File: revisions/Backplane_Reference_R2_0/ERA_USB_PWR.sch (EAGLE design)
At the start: 1 part

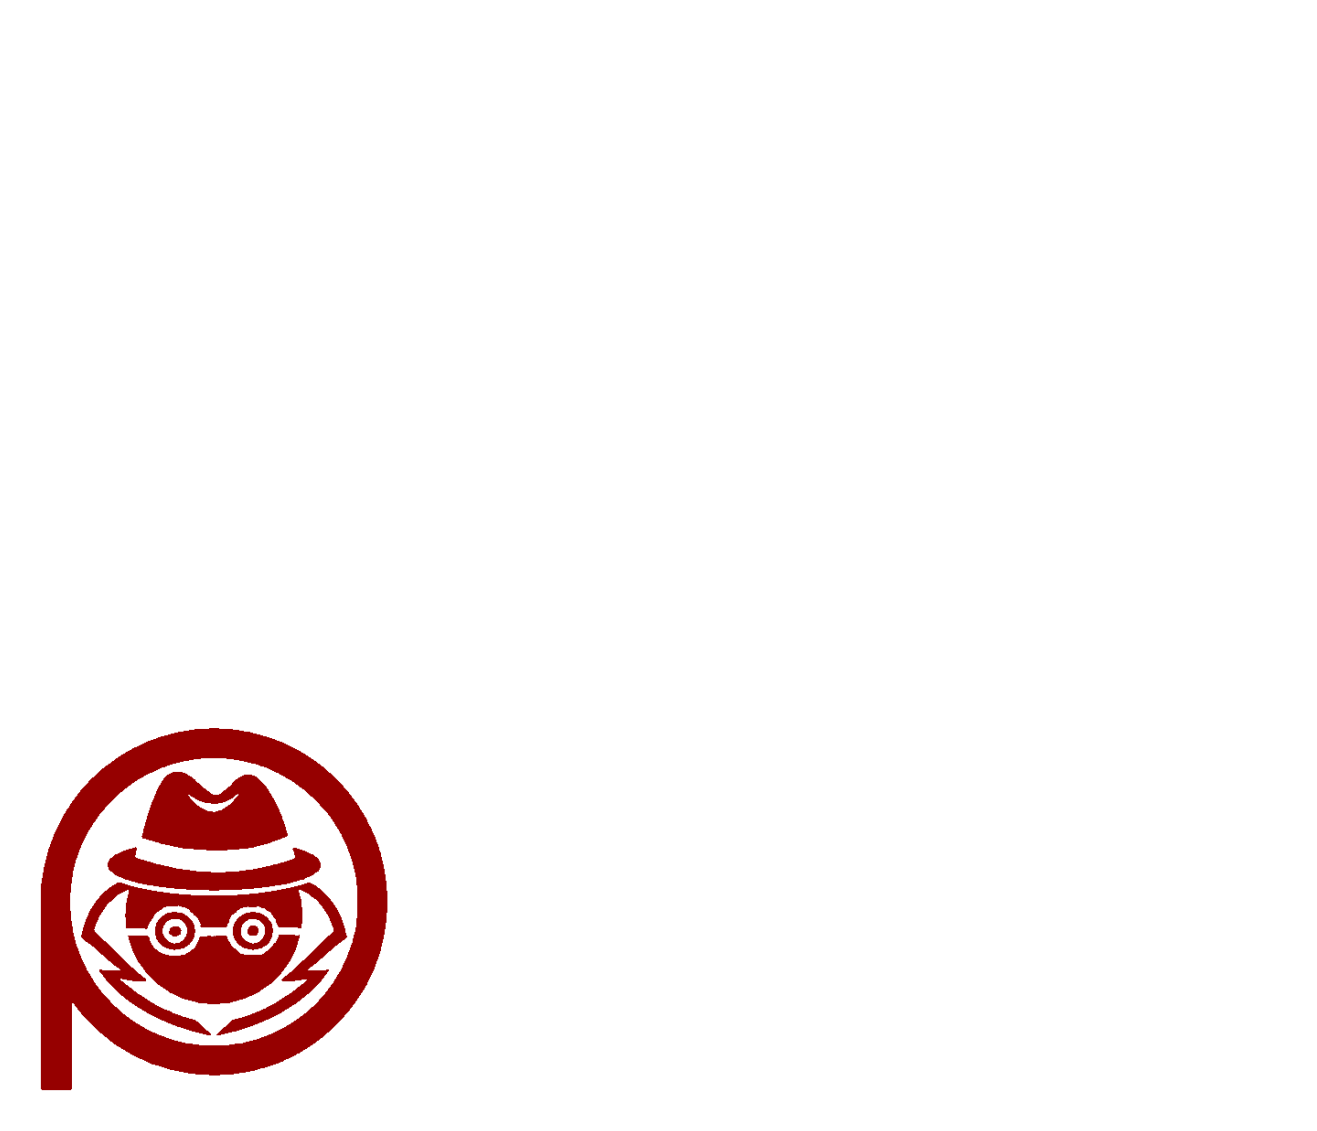
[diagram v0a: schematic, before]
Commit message: Enlarge SwitchMult Front panel holes for easier assembly/operation
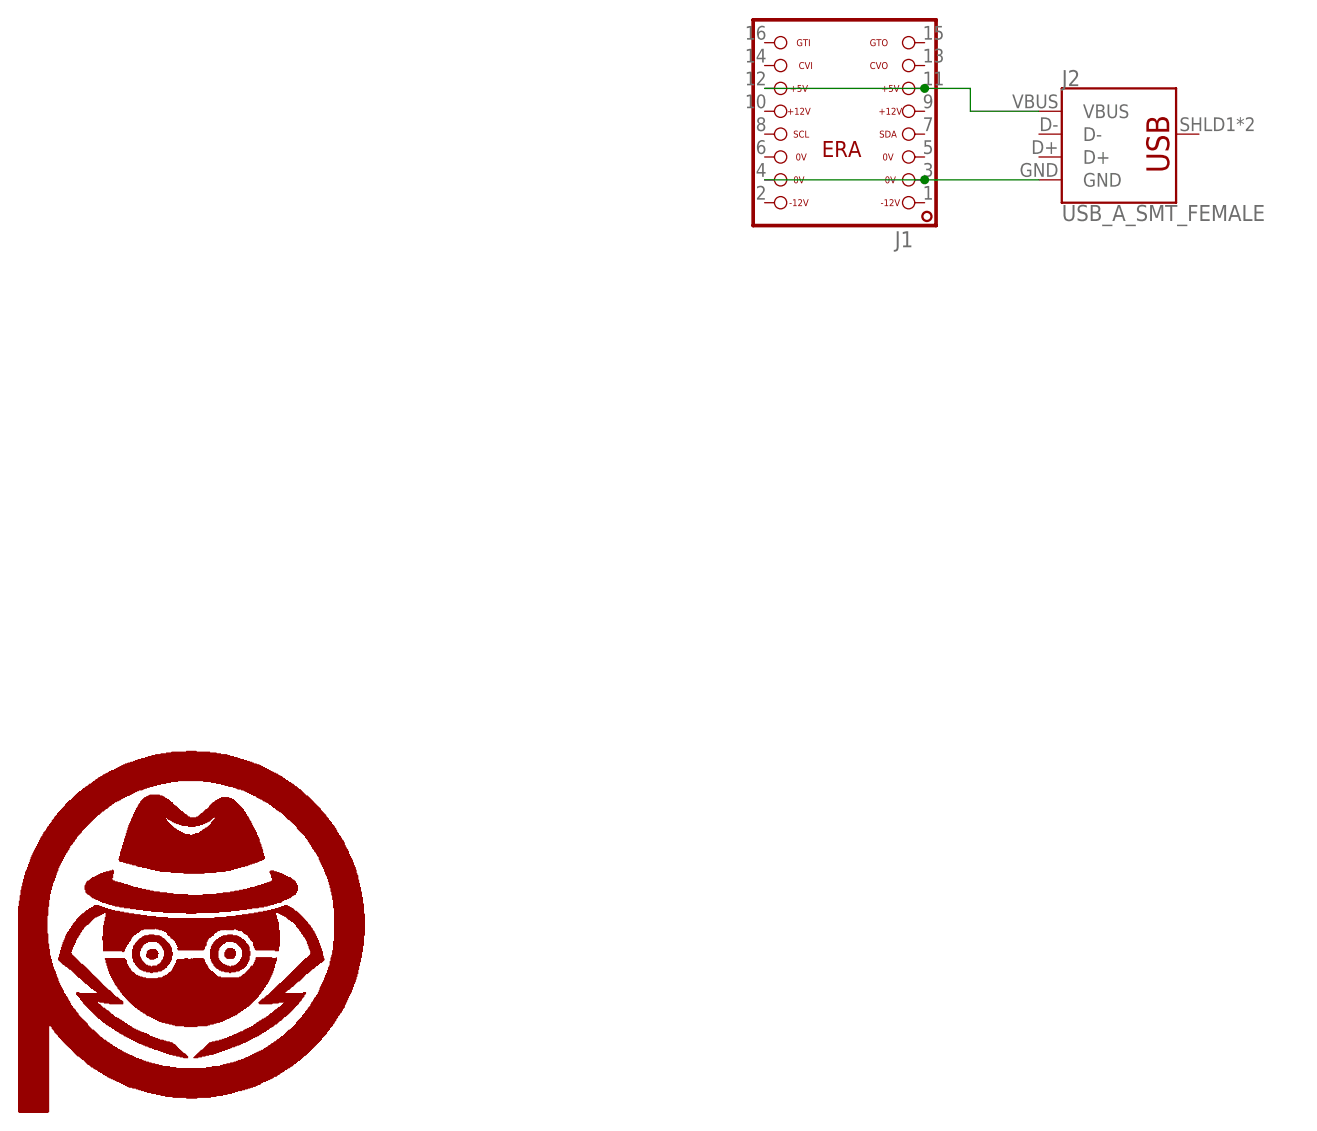
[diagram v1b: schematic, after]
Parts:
- added J1: ERA_16PIN-NOSILK, ERA:ERA_16PIN-NOSILK
- added J2: USB_A_SMT_FEMALE, SparkFun-Connectors:USB_A_SMT_FEMALE
- added U$2: PA_LOGO_SYMSMALL, PatternAgents-Logos:PA_LOGO_SYMSMALL
- U$1: value PA_LOGO_SYMLARGE -> PA_LOGO_SYMSMALL; device PatternAgents-Logos:PA_LOGO_SYMLARGE -> PatternAgents-Logos:PA_LOGO_SYMSMALL
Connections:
- new net GND: J1.3, J1.4, J2.GND
- new net N$2: J1.11, J1.12, J2.VBUS
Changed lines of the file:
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@@
 <layer number="2" name="Route2" color="1" fill="3" visible="no" active="no"/>
 <layer number="3" name="Route3" color="4" fill="3" visible="no" active="no"/>
+<layer number="4" name="Route4" color="1" fill="4" visible="no" active="no"/>
+<layer number="5" name="Route5" color="4" fill="4" visible="no" active="no"/>
+<layer number="6" name="Route6" color="1" fill="8" visible="no" active="no"/>
+<layer number="7" name="Route7" color="4" fill="8" visible="no" active="no"/>
+<layer number="8" name="Route8" color="1" fill="2" visible="no" active="no"/>
+<layer number="9" name="Route9" color="4" fill="2" visible="no" active="no"/>
+<layer number="10" name="Route10" color="1" fill="7" visible="no" active="no"/>
+<layer number="11" name="Route11" color="4" fill="7" visible="no" active="no"/>
+<layer number="12" name="Route12" color="1" fill="5" visible="no" active="no"/>
+<layer number="13" name="Route13" color="4" fill="5" visible="no" active="no"/>
 <layer number="14" name="Route14" color="1" fill="6" visible="no" active="no"/>
 <layer number="15" name="Route15" color="4" fill="6" visible="no" active="no"/>
@@
 <layer number="56" name="wert" color="7" fill="1" visible="no" active="no"/>
 <layer number="57" name="tCAD" color="7" fill="1" visible="no" active="no"/>
-<layer number="58" name="bCAD" color="11" fill="1" visible="no" active="no"/>
 <layer number="59" name="tCarbon" color="7" fill="1" visible="no" active="no"/>
 <layer number="60" name="bCarbon" color="7" fill="1" visible="no" active="no"/>
@@
 <layer number="97" name="Info" color="7" fill="1" visible="yes" active="yes"/>
 <layer number="98" name="Guide" color="6" fill="1" visible="yes" active="yes"/>
-<layer number="99" name="SpiceOrder" color="5" fill="1" visible="no" active="yes"/>
+<layer number="99" name="SpiceOrder" color="7" fill="1" visible="yes" active="yes"/>
 <layer number="100" name="Muster" color="7" fill="1" visible="no" active="yes"/>
 <layer number="101" name="Patch_Top" color="7" fill="1" visible="no" active="yes"/>
@@
 <layer number="115" name="ReferenceISLANDS" color="7" fill="1" visible="yes" active="yes"/>
 <layer number="116" name="Patch_BOT" color="7" fill="1" visible="no" active="yes"/>
-<layer number="117" name="BACKMAAT1" color="7" fill="1" visible="no" active="no"/>
 <layer number="118" name="Rect_Pads" color="7" fill="1" visible="yes" active="yes"/>
-<layer number="119" name="KAP_TEKEN" color="7" fill="1" visible="no" active="no"/>
-<layer number="120" name="KAP_MAAT1" color="7" fill="1" visible="no" active="no"/>
 <layer number="121" name="_tsilk" color="7" fill="1" visible="no" active="yes"/>
 <layer number="122" name="_bsilk" color="7" fill="1" visible="no" active="yes"/>
@@
 <layer number="128" name="_bValues" color="7" fill="1" visible="no" active="yes"/>
 <layer number="129" name="Mask" color="7" fill="1" visible="yes" active="yes"/>
-<layer number="130" name="SMDSTROOK" color="7" fill="1" visible="no" active="no"/>
 <layer number="131" name="tAdjust" color="7" fill="1" visible="no" active="yes"/>
 <layer number="132" name="bAdjust" color="7" fill="1" visible="no" active="yes"/>
-<layer number="133" name="bottom_silk" color="7" fill="1" visible="no" active="no"/>
-<layer number="134" name="silk_top" color="7" fill="1" visible="no" active="no"/>
-<layer number="135" name="silk_bottom" color="7" fill="1" visible="no" active="no"/>
-<layer number="136" name="silktop" color="7" fill="1" visible="yes" active="yes"/>
-<layer number="137" name="silkbottom" color="7" fill="1" visible="yes" active="yes"/>
 <layer number="144" name="Drill_legend" color="7" fill="1" visible="no" active="yes"/>
 <layer number="145" name="DrillLegend_01-02" color="7" fill="1" visible="yes" active="yes"/>
@@
 <layer number="154" name="FabDoc2" color="7" fill="1" visible="yes" active="yes"/>
 <layer number="155" name="FabDoc3" color="7" fill="1" visible="yes" active="yes"/>
-<layer number="190" name="testFixtureBottom" color="10" fill="1" visible="yes" active="yes"/>
-<layer number="191" name="testFixtureUpper" color="14" fill="1" visible="yes" active="yes"/>
 <layer number="199" name="Contour" color="7" fill="1" visible="no" active="yes"/>
 <layer number="200" name="200bmp" color="10" fill="1" visible="yes" active="yes"/>
@@
 <layer number="230" name="230bmp" color="7" fill="1" visible="yes" active="yes"/>
 <layer number="231" name="231bmp" color="7" fill="1" visible="yes" active="yes"/>
-<layer number="232" name="Eagle3D_PG2" color="7" fill="1" visible="no" active="no"/>
-<layer number="233" name="Eagle3D_PG3" color="7" fill="1" visible="no" active="no"/>
+<layer number="232" name="Eagle3D_PG2" color="7" fill="1" visible="yes" active="yes"/>
+<layer number="233" name="Eagle3D_PG3" color="7" fill="1" visible="yes" active="yes"/>
 <layer number="248" name="Housing" color="7" fill="1" visible="no" active="yes"/>
 <layer number="249" name="Edge" color="7" fill="1" visible="no" active="yes"/>
@@
 <parts>
 <part name="FRAME1" library="PatternAgents-Beautify" deviceset="FRAME_ASIZE_LANDSCAPE" device=""/>
-<part name="U$1" library="PatternAgents-Logos" deviceset="PA_LOGO_SYM" device="LARGE" value="PA_LOGO_SYMLARGE"/>
+<part name="J2" library="SparkFun-Connectors" deviceset="USB_A" device="_SMT_FEMALE"/>
+<part name="J1" library="ERA" deviceset="ERA_16PIN" device="-NOSILK"/>
+<part name="U$1" library="PatternAgents-Logos" deviceset="PA_LOGO_SYM" device="SMALL"/>
+<part name="U$2" library="PatternAgents-Logos" deviceset="PA_LOGO_SYM" device="SMALL"/>
 </parts>
 <sheets>
@@
 <instance part="FRAME1" gate="G$2" x="172.72" y="0"/>
 <instance part="FRAME1" gate="G$1" x="0" y="0"/>
-<instance part="U$1" gate="G$1" x="33.02" y="25.4"/>
+<instance part="J2" gate="G$1" x="132.08" y="111.76"/>
+<instance part="J1" gate="J1" x="104.14" y="114.3"/>
+<instance part="U$1" gate="G$1" x="30.48" y="22.86"/>
+<instance part="U$2" gate="G$1" x="30.48" y="22.86"/>
 </instances>
 <busses>
 </busses>
 <nets>
+<net name="GND" class="0">
+<segment>
+<pinref part="J2" gate="G$1" pin="GND"/>
+<pinref part="J1" gate="J1" pin="3"/>
+<wire x1="124.46" y1="109.22" x2="111.76" y2="109.22" width="0.1524" layer="91"/>
+<pinref part="J1" gate="J1" pin="4"/>
+<wire x1="111.76" y1="109.22" x2="93.98" y2="109.22" width="0.1524" layer="91"/>
+<junction x="111.76" y="109.22"/>
+</segment>
+</net>
+<net name="N$2" class="0">
+<segment>
+<pinref part="J2" gate="G$1" pin="VBUS"/>
+<wire x1="124.46" y1="116.84" x2="116.84" y2="116.84" width="0.1524" layer="91"/>
+<wire x1="116.84" y1="116.84" x2="116.84" y2="119.38" width="0.1524" layer="91"/>
+<pinref part="J1" gate="J1" pin="11"/>
+<wire x1="116.84" y1="119.38" x2="111.76" y2="119.38" width="0.1524" layer="91"/>
+<pinref part="J1" gate="J1" pin="12"/>
+<wire x1="111.76" y1="119.38" x2="93.98" y2="119.38" width="0.1524" layer="91"/>
+<junction x="111.76" y="119.38"/>
+</segment>
+</net>
 </nets>
 </sheet>
